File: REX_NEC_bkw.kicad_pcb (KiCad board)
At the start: 2 copper layers, 16.3 x 34 mm, 9 parts, among them J1 DIP28 legs 27C256, J2 JTAG, J3 PRG, U1 XCR3064-VQ44, U2 29F800, U3 LP2980

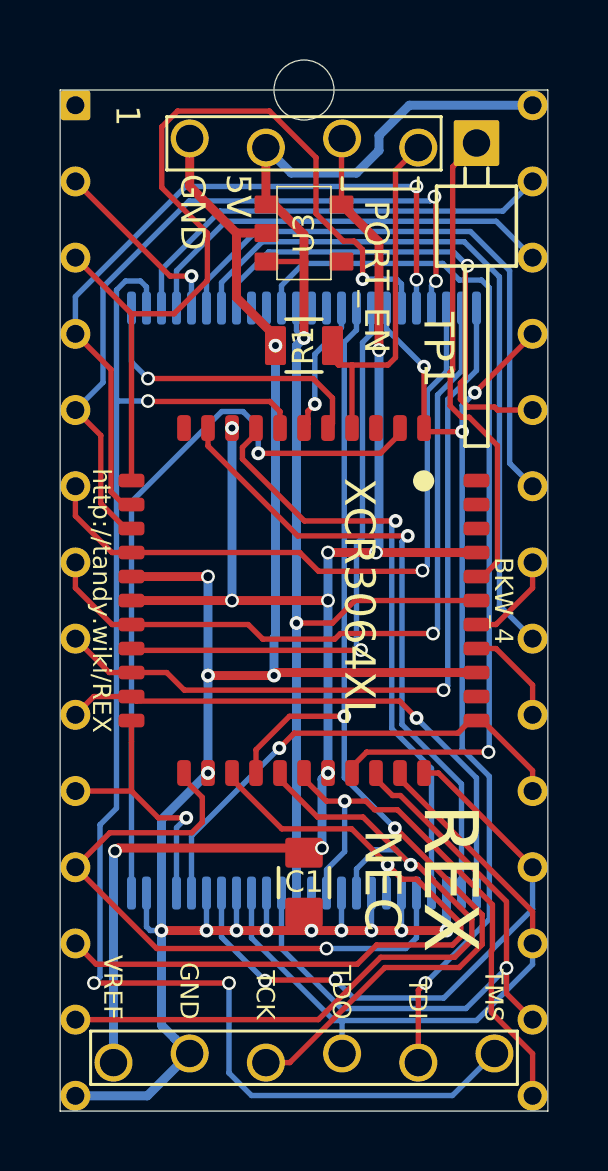
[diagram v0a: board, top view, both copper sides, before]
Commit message: Less expensive manufacturing tolerances. Rename to REX Classic.
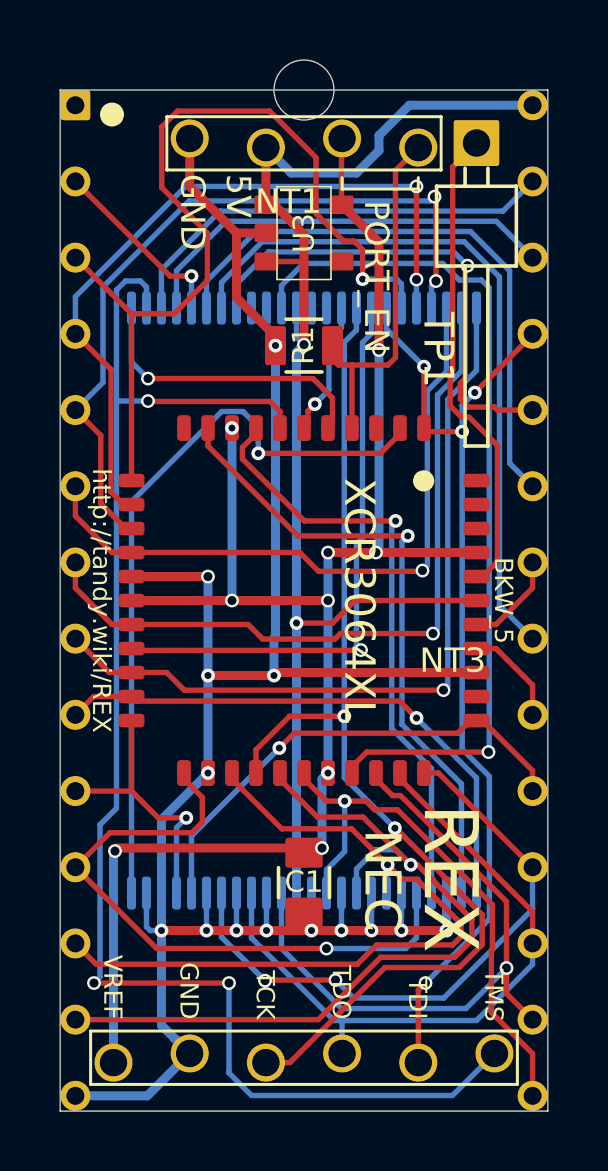
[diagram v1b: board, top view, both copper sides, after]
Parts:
- added NT1: Net-Tie_2, 000_LOCAL:Net_Tie_2_0.18mm, F.Cu at (145.0, 86.0)
- added NT2: Net-Tie_2, 000_LOCAL:Net_Tie_2_0.18mm, B.Cu at (145.3, 88.3)
- added NT3: Net-Tie_2, 000_LOCAL:Net_Tie_2_0.18mm, F.Cu at (150.5, 97.3)
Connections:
- U1 pad 39: +5V -> /~RESET_U1
- U2 pad 12: +5V -> /~RESET_U2
- U3 pad 3: (no net) -> /EN
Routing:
- net +5V: track 44.8 -> 42.3 mm
- net /~RESET_U2: track 0.00 -> 0.69 mm
- net /~RESET_U1: track 0.00 -> 0.69 mm
- net /EN: track 0.00 -> 0.63 mm
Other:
- board text added: "BKW_5"
- board text removed: "1"
- board text removed: "BKW_4"

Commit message: rename pcb2molex8878 to Molex78805_PCB
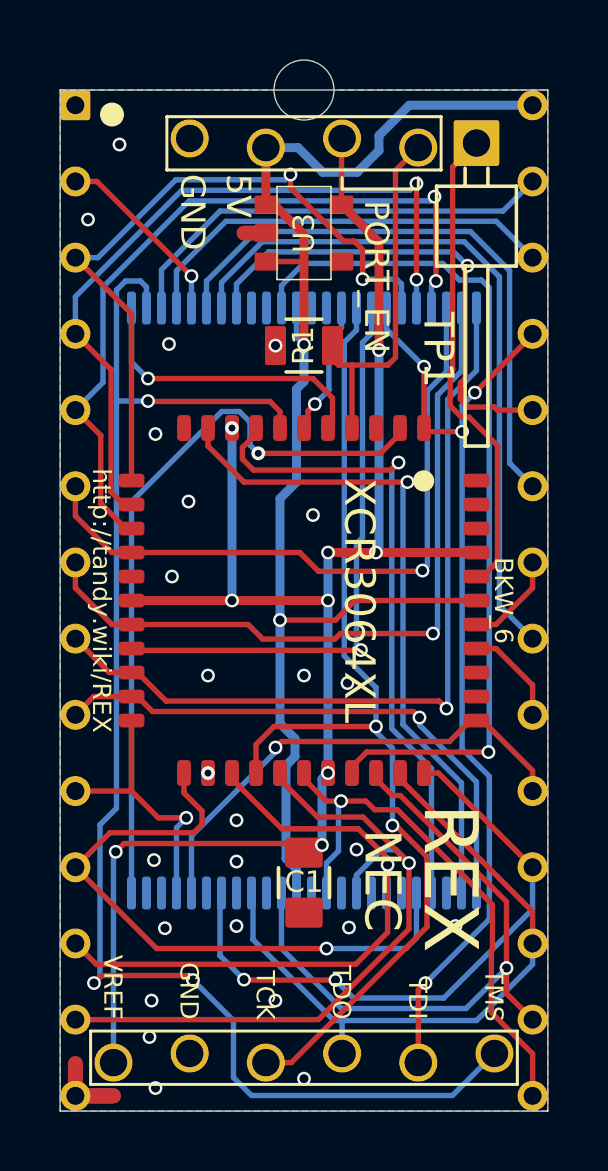
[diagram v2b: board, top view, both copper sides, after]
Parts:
- U2: value 29F800 -> 29F800BB
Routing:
- net GND: track 76.2 -> 4.37 mm, vias 14 -> 25
- net /eA7: track 30.0 -> 23.4 mm, vias 1 -> 2
- net /eD1: track 24.7 -> 21.0 mm
- net /eD2: track 26.6 -> 23.1 mm
- net /TCK: track 36.3 -> 34.4 mm
- net /_~OE: track 20.2 -> 21.7 mm
- net +5V: track 42.3 -> 43.5 mm
- net /_~CE: track 21.3 -> 22.3 mm
- net /eA2: track 26.2 -> 27.1 mm
- added copper zone on B.Cu, net GND
- added copper zone on F.Cu, net GND
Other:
- board text added: "BKW_6"
- board text removed: "BKW_5"

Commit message: clearances
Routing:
- net /TMS: track 48.3 -> 47.8 mm
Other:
- board text added: "BKW_7"
- board text removed: "BKW_6"

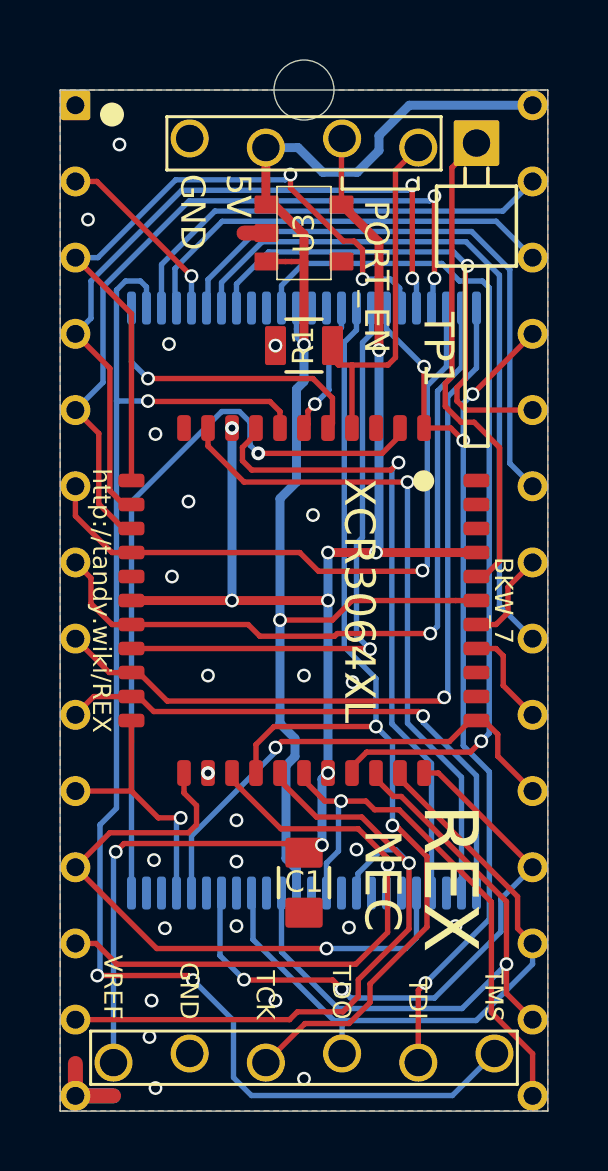
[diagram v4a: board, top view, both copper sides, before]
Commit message: clearances, remove pointless busses in schematic
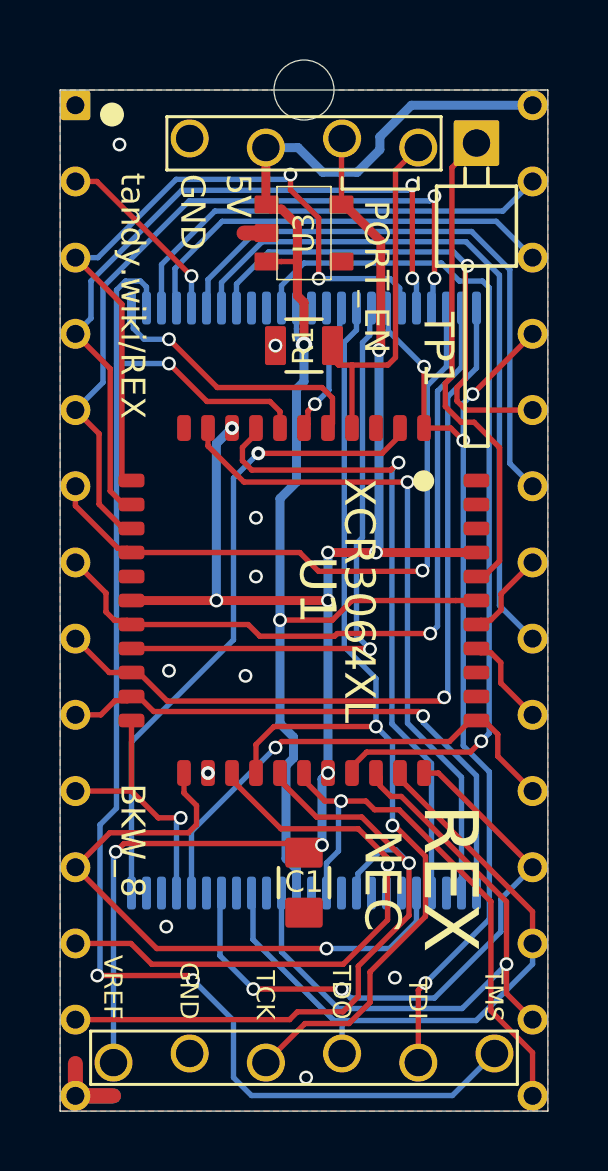
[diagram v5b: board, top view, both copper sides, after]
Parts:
- C1: value C-USC0805 -> 1u
- U1: footprint 000_LOCAL:QFP44 -> 000_LOCAL:VQFP44
- U2: value 29F800BB -> 29F800
- moved NT1 0.33 mm to (144.7, 86.0)
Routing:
- net /_A16: track 24.8 -> 21.6 mm
- net /eA7: track 23.3 -> 24.1 mm
- net /_A15: track 10.1 -> 9.37 mm
- net /TMS: track 47.8 -> 48.3 mm
- net GND: vias 25 -> 10
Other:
- board text added: "BKW_8"
- board text added: "tandy.wiki/REX"
- board text removed: "BKW_7"
- board text removed: "http://tandy.wiki/REX"
